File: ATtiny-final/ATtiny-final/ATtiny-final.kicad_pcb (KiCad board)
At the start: 2 copper layers, 19.5 x 19.4 mm, 8 parts, among them J1 Conn_01x07_Male, J2 Conn_01x07_Male, U1 ATtiny424-X

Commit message: platinen angepasst
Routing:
- added copper zone on B.Cu, net GND
- added copper zone on In1.Cu, net GND
- added copper zone on In2.Cu, net GND
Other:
- copper layers 2 -> 4
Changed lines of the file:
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@@
   (layers
     (0 "F.Cu" signal)
+    (1 "In1.Cu" signal)
+    (2 "In2.Cu" signal)
     (31 "B.Cu" signal)
     (32 "B.Adhes" user "B.Adhesive")
@@
       (layer "F.Mask" (type "Top Solder Mask") (thickness 0.01))
       (layer "F.Cu" (type "copper") (thickness 0.035))
-      (layer "dielectric 1" (type "core") (thickness 1.51) (material "FR4") (epsilon_r 4.5) (loss_tangent 0.02))
+      (layer "dielectric 1" (type "prepreg") (thickness 0.1) (material "FR4") (epsilon_r 4.5) (loss_tangent 0.02))
+      (layer "In1.Cu" (type "copper") (thickness 0.035))
+      (layer "dielectric 2" (type "core") (thickness 1.24) (material "FR4") (epsilon_r 4.5) (loss_tangent 0.02))
+      (layer "In2.Cu" (type "copper") (thickness 0.035))
+      (layer "dielectric 3" (type "prepreg") (thickness 0.1) (material "FR4") (epsilon_r 4.5) (loss_tangent 0.02))
       (layer "B.Cu" (type "copper") (thickness 0.035))
       (layer "B.Mask" (type "Bottom Solder Mask") (thickness 0.01))
@@
     (pad_to_mask_clearance 0)
     (pcbplotparams
-      (layerselection 0x0001000_7fffffff)
+      (layerselection 0x0001000_ffffffff)
       (plot_on_all_layers_selection 0x0000000_00000000)
       (disableapertmacros false)
@@
     (connect_pads (clearance 0.5))
     (min_thickness 0.25) (filled_areas_thickness no)
+    (fill yes (thermal_gap 0.5) (thermal_bridge_width 0.5))
+    (polygon
+      (pts
+        (xy 141.5 89.4)
+        (xy 161 89.4)
+        (xy 161 108.8)
+        (xy 141.5 108.8)
+      )
+    )
+  )
+  (zone (net 1) (net_name "GND") (layers "In1.Cu" "In2.Cu" "B.Cu") (hatch edge 0.5)
+    (priority 1)
+    (connect_pads (clearance 0.5))
+    (min_thickness 0.25) (filled_areas_thickness no)

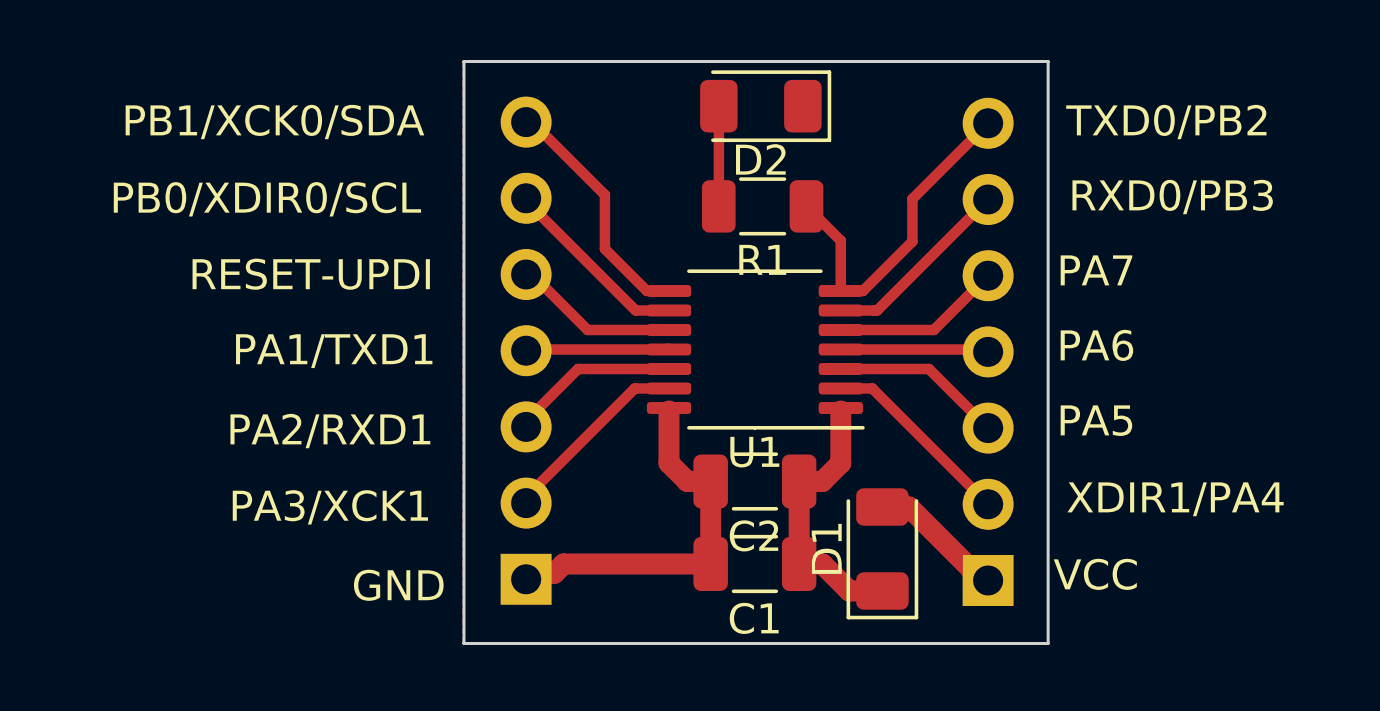
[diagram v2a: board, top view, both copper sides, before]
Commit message: punkt bei pin 1 der ics hinzugefügt
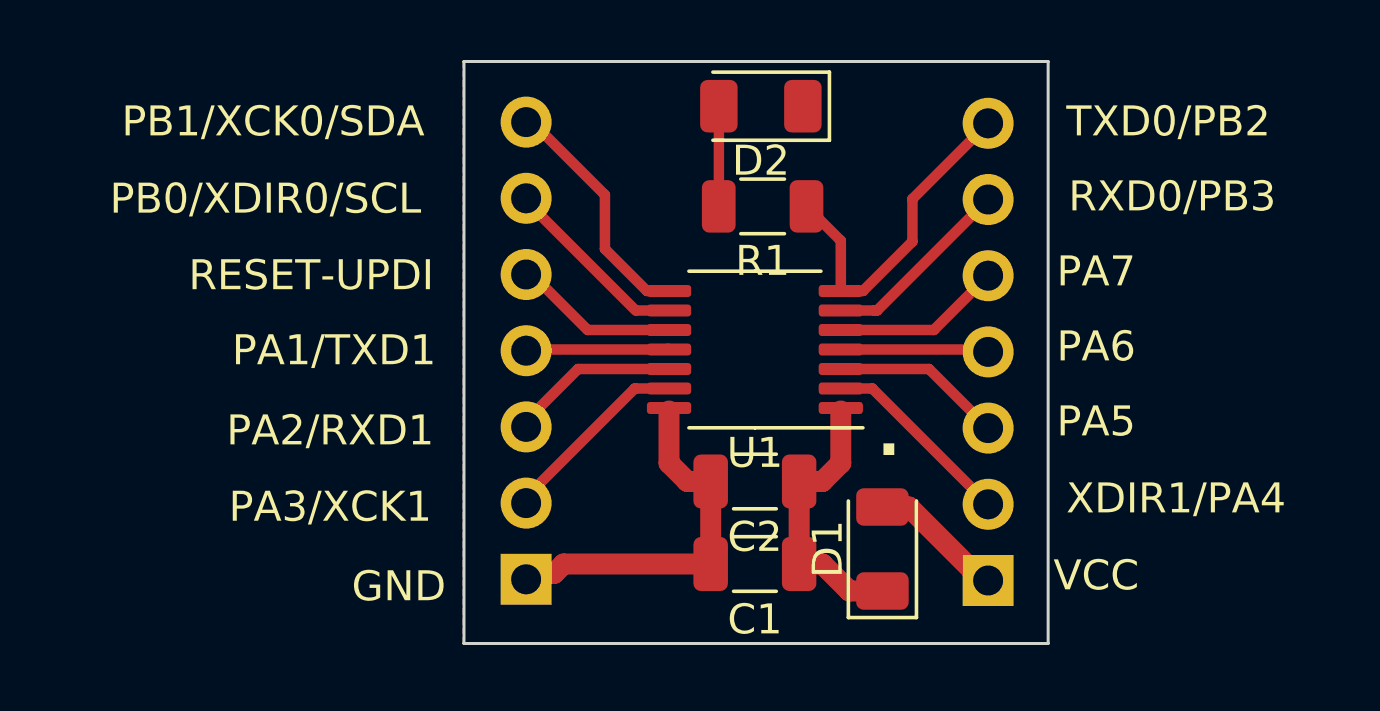
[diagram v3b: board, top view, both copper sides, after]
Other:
- board text added: "."
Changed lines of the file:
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@@
     (pad_to_mask_clearance 0)
     (pcbplotparams
-      (layerselection 0x0001000_ffffffff)
+      (layerselection 0x0001020_ffffffff)
       (plot_on_all_layers_selection 0x0000000_00000000)
       (disableapertmacros false)
@@
     (effects (font (size 1 1) (thickness 0.15)))
   )
+  (gr_text "." (at 155.3 102.7) (layer "F.SilkS")
+    (effects (font (size 1.5 1.5) (thickness 0.3) bold) (justify left bottom))
+  )
   (gr_text "GND" (at 139.357 106.895819) (layer "F.SilkS")
